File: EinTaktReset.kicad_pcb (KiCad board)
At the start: 2 copper layers, 100 x 160 mm, 60 parts, among them IC1 74LS624, J1 3PinTerminalBlocktg, J2 3PinTerminalBlocktg, J3 2PinTerminalBlocktg, J4 3PinTerminalBlocktg, J5 2PinTerminalBlocktg, P1 CONN_02X10, P4 CONN_02X10, SW1 SWITCH_INV, SW10 SPST, SW11 SPST, SW12 SPST, SW13 SPST, SW2 SWITCH_INV, SW3 SPST, SW4 SPST, SW5 SPST, SW6 SWITCH_INV, SW7 SPST, SW8 SPST, SW9 SPST, U1 74LS132, U2 74540En, U3 74HCT541_PWR, U4 74LS32, U5 74LS00

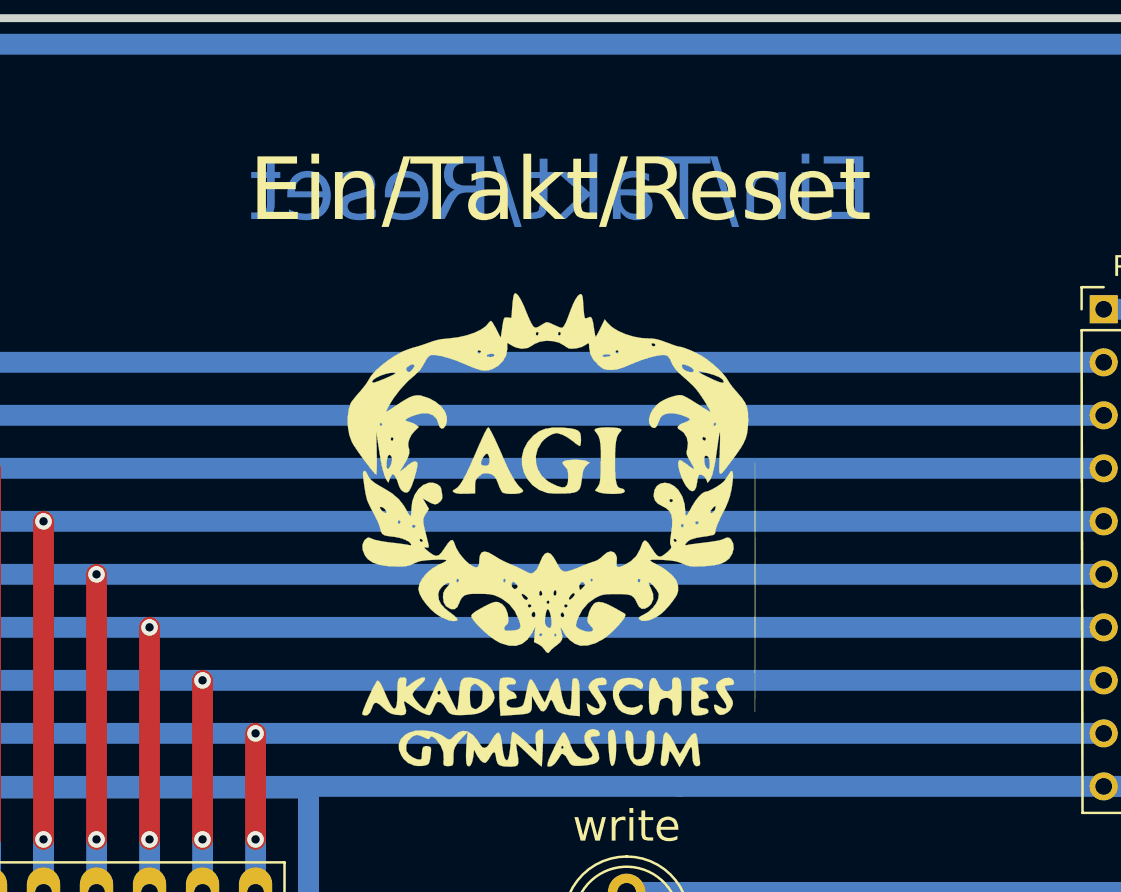
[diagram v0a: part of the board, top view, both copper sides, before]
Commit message: Speicher Layout EinTaktReset VCO
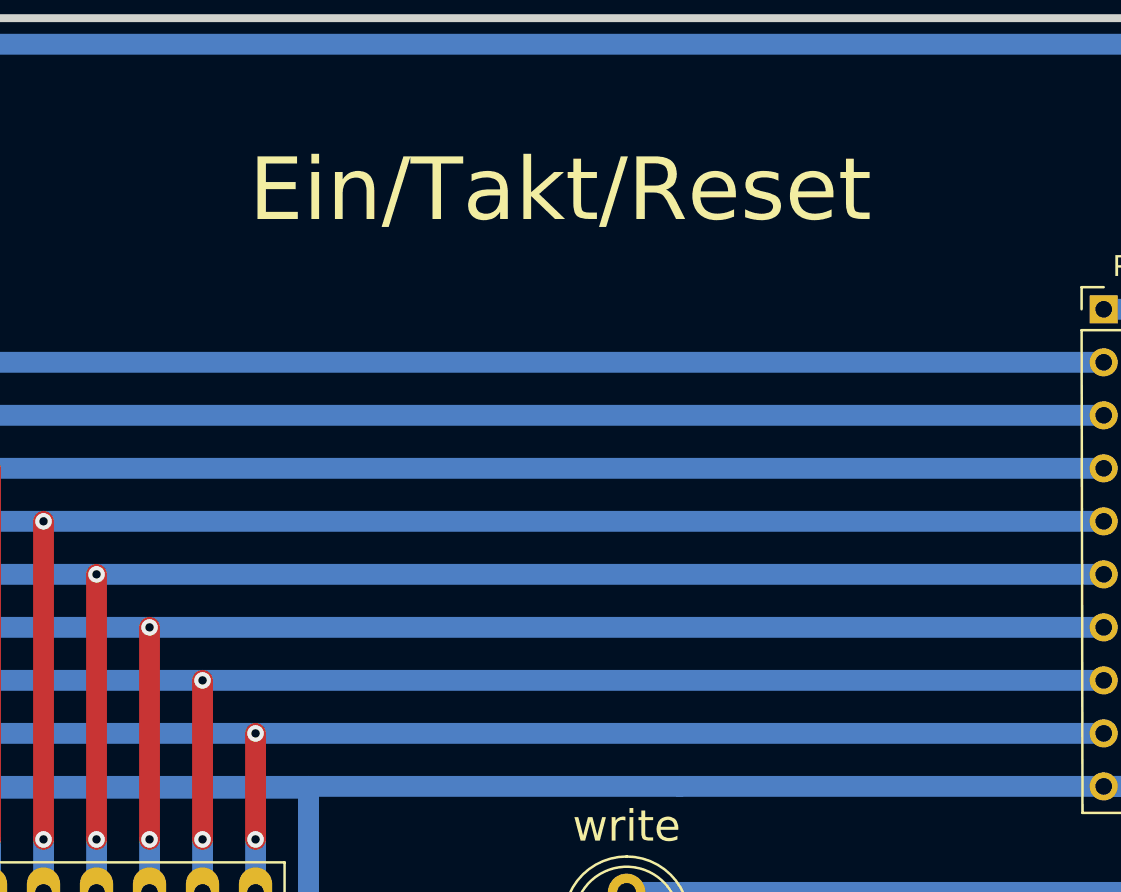
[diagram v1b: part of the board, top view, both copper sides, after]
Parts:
- removed G***: LOGO, allBonsaiFootprintsLibs:agi5

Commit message: EinTaktReset
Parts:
- removed IC1: 74LS624, Housings_DIP:DIP-14_W7.62mm_Socket_LongPads
- removed the REF** at (146.1, 186.7)
- added C10: C, Capacitor_THT:C_Disc_D10.0mm_W2.5mm_P5.00mm, F.Cu at (73.7, 114.2)
- added C11: CP, Capacitor_THT:CP_Radial_D8.0mm_P2.50mm, F.Cu at (73.7, 30.5)
- added C12: 100n, Capacitor_THT:C_Disc_D10.0mm_W2.5mm_P5.00mm, F.Cu at (93.3, 168.3)
- added C13: 100n, Capacitor_THT:C_Disc_D10.0mm_W2.5mm_P5.00mm, F.Cu at (77.5, 94.0)
- added C14: CP, Capacitor_THT:CP_Radial_D10.0mm_P2.50mm_P5.00mm, F.Cu at (82.9, 121.9)
- added C15: CP, Capacitor_THT:CP_Radial_D10.0mm_P2.50mm_P5.00mm, F.Cu at (82.9, 113.0)
- added J6: Conn_01x02, Connector_Molex:Molex_KK-254_AE-6410-02A_1x02_P2.54mm_Vertical, F.Cu at (132.1, 166.4)
- added R18: 10k, Resistor_THT:R_Axial_DIN0207_L6.3mm_D2.5mm_P10.16mm_Horizontal, F.Cu at (70.5, 90.8)
- added R19: 10k, Resistor_THT:R_Axial_DIN0207_L6.3mm_D2.5mm_P10.16mm_Horizontal, F.Cu at (55.2, 101.0)
- added REF**: EuroBoard160mmX100mm_holes_keepout, bonsai:EuroBoard160mmX100mm_holes_keepout, F.Cu at (38.1, 22.9)
- added U6: 74HC4046, Package_DIP:DIP-16_W7.62mm_Socket_LongPads, F.Cu at (81.3, 100.3)
- C1, C2: footprint Capacitors_ThroughHole:CP_Radial_D5.0mm_P2.00mm -> Capacitor_THT:CP_Radial_D5.0mm_P2.00mm
- C3: value 220 µ -> CP; footprint Capacitors_ThroughHole:CP_Radial_D8.0mm_P3.50mm -> Capacitor_THT:CP_Radial_D10.0mm_P2.50mm_P5.00mm
- C4: value 220µ -> CP; footprint Capacitors_ThroughHole:CP_Radial_D8.0mm_P3.50mm -> Capacitor_THT:CP_Radial_D10.0mm_P2.50mm_P5.00mm
- C5: value 10n -> C; footprint Capacitors_ThroughHole:C_Disc_D3.0mm_W1.6mm_P2.50mm -> Capacitor_THT:C_Disc_D9.0mm_W5.0mm_P5.00mm
- C6, C7, C8, C9: footprint Capacitors_ThroughHole:C_Disc_D10.0mm_W2.5mm_P5.00mm -> Capacitor_THT:C_Disc_D10.0mm_W2.5mm_P5.00mm
- D1, D3: footprint Diodes_ThroughHole:D_DO-35_SOD27_P10.16mm_Horizontal -> Diode_THT:D_A-405_P10.16mm_Horizontal
- D2: footprint LEDs:LED_D5.0mm -> LED_THT:LED_D3.0mm
- DROT1: footprint LEDs:LED_D3.0mm -> LED_THT:LED_D3.0mm
- J1: value 3PinTerminalBlocktg -> Conn_01x02; footprint 3PinTerminalBlocktg -> Connector_Molex:Molex_KK-254_AE-6410-02A_1x02_P2.54mm_Vertical
- J2, J4: value 3PinTerminalBlocktg -> Conn_01x03; footprint 3PinTerminalBlocktg -> Connector_Molex:Molex_KK-254_AE-6410-03A_1x03_P2.54mm_Vertical
- J3: value 2PinTerminalBlocktg -> Conn_01x03; footprint 2PinTerminalBlocktg -> Connector_Molex:Molex_KK-254_AE-6410-03A_1x03_P2.54mm_Vertical
- J5: value 2PinTerminalBlocktg -> Conn_01x02; footprint 2PinTerminalBlocktg -> Connector_Molex:Molex_KK-254_AE-6410-02A_1x02_P2.54mm_Vertical
- P1, P4: footprint tg_foodprint:Pin_Header_Straight_2x10_Pitch2.00mmBonsai.pretty -> Connector_PinHeader_2.54mm:PinHeader_2x10_P2.54mm_Vertical
- R1, R10, R11, R13, R16, R17, R2, R4, R5, R6, R8: footprint Resistors_ThroughHole:R_Axial_DIN0207_L6.3mm_D2.5mm_P10.16mm_Horizontal -> Resistor_THT:R_Axial_DIN0207_L6.3mm_D2.5mm_P10.16mm_Horizontal
- R12, R9: footprint tg_foodprint:R_Axial_DIN0207_L6.3mm_D2.5mm_P12.7mm_Horizontaltg -> Resistor_THT:R_Axial_DIN0207_L6.3mm_D2.5mm_P10.16mm_Horizontal
- R14, R15: footprint tg_bonsai_proj_spec_libs:R_Axial_DIN0207_L6.3mm_D2.5mm_P10.16mm_Horizontal -> Resistor_THT:R_Axial_DIN0207_L6.3mm_D2.5mm_P10.16mm_Horizontal
- R3: footprint tg_foodprint:R_Axial_DIN0207_L6.3mm_D2.5mm_P17.7mm_Horizontaltg -> Resistor_THT:R_Axial_DIN0207_L6.3mm_D2.5mm_P10.16mm_Horizontal
- R7: footprint tg_foodprint:R_Axial_DIN0207_L6.3mm_D2.5mm_P21.59mm_Horizontaltg -> Resistor_THT:R_Axial_DIN0207_L6.3mm_D2.5mm_P10.16mm_Horizontal
- RP1: footprint Housings_SIP:SIP9_Housing_BigPads -> Resistor_THT:R_Array_SIP9
- RV1: value POT -> Poti 10k
- SW1, SW2: value SWITCH_INV -> Digitast; footprint tg_foodprint:SW_PUSH_LCD_E3_SAxxxx_tg_V2 -> bonsai:Switch_Digitast
- SW10, SW11, SW12, SW13, SW5, SW7, SW8, SW9: footprint tg_foodprint:eintakt_tg_SW_CuK_JS202011CQN_DPDT_Straight -> Switches-Walter:switch_100sp5
- SW3, SW4: value SPST -> SW_SPDT; footprint tg_foodprint:eintakt_tg_SW_CuK_JS202011CQN_DPDT_Straight -> Switches-Walter:switch_100sp5
- SW6: value SWITCH_INV -> SW_SPDT; footprint tg_foodprint:eintakt_tg_SW_CuK_JS202011CQN_DPDT_Straight -> Switches-Walter:switch_100sp5
- U1: value 74LS132 -> 74132; footprint Housings_DIP:DIP-14_W7.62mm_Socket_LongPads -> Package_DIP:DIP-14_W7.62mm_Socket_LongPads
- U2: value 74540En -> 74540; footprint Housings_DIP:DIP-20_W7.62mm_Socket_LongPads -> Package_DIP:DIP-20_W7.62mm_Socket_LongPads
- U3: footprint Housings_DIP:DIP-20_W7.62mm_Socket_LongPads -> Package_DIP:DIP-20_W7.62mm_Socket_LongPads
- U4: value 74LS32 -> 7432; footprint Housings_DIP:DIP-14_W7.62mm_Socket_LongPads -> Package_DIP:DIP-14_W7.62mm_Socket_LongPads
- U5: value 74LS00 -> 7400; footprint Housings_DIP:DIP-14_W7.62mm_Socket_LongPads -> Package_DIP:DIP-14_W7.62mm_Socket_LongPads
- moved J1 142.0 mm to (50.2, 29.2), turned to 0 degrees
- moved J3 117.9 mm to (132.1, 125.1), turned to 270 degrees
- moved R10 46.4 mm to (118.1, 138.4), turned to 90 degrees
- moved R16 44.6 mm to (53.3, 119.4)
- moved R11 40.2 mm to (121.9, 135.3), turned to 90 degrees
- moved R7 39.1 mm to (121.9, 61.0), turned to 180 degrees
- moved J2 33.6 mm to (132.1, 81.9)
- moved SW4 32.2 mm to (47.0, 96.5)
- moved SW3 29.6 mm to (47.0, 114.0)
- moved R17 28.5 mm to (94.0, 88.9), turned to 180 degrees
- moved R9 27.7 mm to (94.6, 155.6), turned to 0 degrees
- moved RV1 25.1 mm to (65.4, 99.1), turned to 90 degrees
- moved R13 23.6 mm to (97.2, 158.8), turned to 0 degrees
- moved SW1 23.0 mm to (47.0, 161.9), turned to 90 degrees
- moved R15 21.9 mm to (59.7, 131.4), turned to 270 degrees
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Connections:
- C4 pad 2: Net-(C4-Pad2) -> Net-(C10-Pad2)
- C5 pad 1: Net-(C4-Pad2) -> Net-(C3-Pad2)
- C5 pad 2: Net-(C5-Pad2) -> Net-(C10-Pad2)
- J1 pad 1: en-ln1 -> GND
- J1 pad 2: en-ln2 -> VCC
- J3 pad 1: GND -> en-ln1
- J3 pad 2: VCC -> en-ln2
- J5 pad 1: clrPC -> Net-(J5-Pad1)
- J5 pad 2: clrAkku -> clrPC
- P1 pad 11: GND -> /a4
- P1 pad 13: GND -> /a5
- P1 pad 15: GND -> /a6
- P1 pad 17: GND -> /a7
- P1 pad 2: /a0 -> GND
- P1 pad 3: /a1 -> /a0
- P1 pad 4: /a2 -> GND
- P1 pad 5: /a3 -> /a1
- P1 pad 6: /a4 -> GND
- P1 pad 7: /a5 -> /a2
- P1 pad 8: /a6 -> GND
- P1 pad 9: /a7 -> /a3
- P4 pad 11: GND -> /a4
- P4 pad 13: GND -> /a5
- P4 pad 15: GND -> /a6
- P4 pad 17: GND -> /a7
- P4 pad 2: /a0 -> GND
- P4 pad 3: /a1 -> /a0
- P4 pad 4: /a2 -> GND
- P4 pad 5: /a3 -> /a1
- P4 pad 6: /a4 -> GND
- P4 pad 7: /a5 -> /a2
- P4 pad 8: /a6 -> GND
- P4 pad 9: /a7 -> /a3
- R11 pad 1: en-ln1 -> VCC
- R11 pad 2: VCC -> en-ln1
- R16 pad 2: Net-(IC1-Pad5) -> Net-(R16-Pad2)
- R17 pad 2: VCC -> GND
- RV1 pad 1: VCC -> Net-(R18-Pad2)
- RV1 pad 3: GND -> Net-(R19-Pad1)
- SW1 pad 2: (no net) -> Net-(SW1-Pad2)
- SW3 pad 1: GND -> Net-(R16-Pad2)
- SW3 pad 2: Net-(IC1-Pad5) -> GND
- SW3 pad 3: (no net) -> Net-(SW3-Pad3)
- SW4 pad 1: Net-(C5-Pad2) -> Net-(C10-Pad1)
- SW4 pad 3: (no net) -> Net-(SW4-Pad3)
- SW6 pad 1: auto -> VCC
- SW6 pad 2: GND -> auto
- U2 pad 20: (no net) -> VCC
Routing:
- net GND: track 1113.8 -> 799.3 mm
- net Net-(IC1-Pad5): track 109.1 -> 0.00 mm
- net Net-(C10-Pad1): track 0.00 -> 77.3 mm
- net VCC: track 624.5 -> 557.3 mm, vias 8 -> 0
- net Net-(C10-Pad2): track 0.00 -> 53.6 mm
- net Net-(C5-Pad2): track 51.0 -> 0.00 mm, vias 2 -> 0
- net Net-(R16-Pad2): track 0.00 -> 50.0 mm
- net auto: track 93.4 -> 47.0 mm
- net Net-(U5-Pad2): track 88.5 -> 47.8 mm, vias 2 -> 0
- net Net-(U3-Pad1): track 197.6 -> 159.0 mm, vias 2 -> 0
- net Net-(C3-Pad2): track 17.7 -> 50.6 mm
- net enDEC: track 135.7 -> 103.8 mm
- net Net-(U1-Pad12): track 112.2 -> 80.8 mm
- net Net-(R7-Pad1): track 19.4 -> 49.1 mm
- net Net-(C4-Pad2): track 28.9 -> 0.00 mm
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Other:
- board text added: "0"
- board text added: "1"
- board text added: "2"
- board text added: "3"
- board text added: "4"
- board text added: "5"
- board text added: "6"
- board text added: "7"
- board text added: "clrAkku"
- board text added: "clrPc"
- board text removed: "+"
- board text removed: "-"
- board text removed: "CLK"
- board text removed: "ClrAkku"
- board text removed: "ClrPC"
- board text removed: "Dauer"
- board text removed: "Einzel"
- board text removed: "Hand"
- board text removed: "Steuerwerk"
- board text removed: "auto"
- board text removed: "~clrMPC"
- board text removed: "~en-IN1"
- board text removed: "~en-IN2"
- board text removed: "~enAkku"
- board text removed: "~enCU"
- board text removed: "~enDEC"
- board text removed: "~loadIR"

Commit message: EinTaktReset
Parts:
- C5: footprint Capacitor_THT:C_Disc_D9.0mm_W5.0mm_P5.00mm -> Capacitor_THT:CP_Axial_L30.0mm_D12.5mm_P35.00mm_Horizontal
- moved C10 30.2 mm to (103.4, 119.4), turned to 180 degrees
- moved C14 21.9 mm to (102.6, 112.4), turned to 90 degrees
- moved R7 17.3 mm to (132.1, 74.9), turned to 90 degrees
- moved C5 15.3 mm to (58.3, 125.7), turned to 0 degrees
- moved C4 11.8 mm to (76.8, 112.4)
- moved R10 10.3 mm to (120.0, 128.3), turned to 180 degrees
- moved R11 10.3 mm to (120.0, 125.1), turned to 180 degrees
- moved U5 9.61 mm to (74.9, 148.0)
- moved C3 9.58 mm to (64.1, 112.4), turned to 90 degrees
- moved C7 9.53 mm to (67.9, 141.7)
- moved SW2 9.52 mm to (47.0, 141.6)
- moved R15 8.28 mm to (59.1, 139.7)
- moved R14 8.26 mm to (62.9, 149.9)
- moved C15 7.65 mm to (90.5, 112.4)
- moved R16 7.62 mm to (53.3, 127.0)
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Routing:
- net VCC: track 557.3 -> 620.6 mm
- net GND: track 799.3 -> 827.5 mm
- net enDEC: track 103.8 -> 127.9 mm, vias 0 -> 2
- net Net-(U1-Pad12): track 80.8 -> 102.3 mm, vias 0 -> 1
- net Net-(D2-Pad1): track 4.45 -> 23.7 mm
- net Net-(R7-Pad1): track 49.1 -> 35.3 mm
- net Net-(R16-Pad2): track 50.0 -> 62.4 mm
- net Net-(U4-Pad13): track 56.6 -> 67.5 mm
- net Net-(U3-Pad1): track 159.0 -> 168.0 mm
- net Net-(D1-Pad2): track 49.7 -> 40.9 mm
- net Net-(R14-Pad2): track 57.5 -> 48.9 mm
- net /a7: track 105.6 -> 97.4 mm
- net Net-(R15-Pad1): track 104.5 -> 96.5 mm
- net Net-(U5-Pad2): track 47.8 -> 55.7 mm
- net /a6: track 105.1 -> 98.2 mm
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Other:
- rule pad_to_mask_clearance: 0.2 -> 0.08
- board text added: "+"
- board text added: "-"
- board text added: "CLK"
- board text added: "Hand"
- board text added: "Steuer- werk"
- board text added: "aus"
- board text added: "kont. Takt ein"
- board text added: "~auto"
- board text added: "~clrMPC"
- board text added: "~enCu"
- board text added: "~enDec"
- board text added: "~enIn1"
- board text added: "~enIn2"
- board text added: "~readIR"
- board text added: "~writeAccu"
